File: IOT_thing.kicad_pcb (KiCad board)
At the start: 2 copper layers, 100 x 100 mm, 64 parts, among them J1 USB_C_Receptacle_USB2.0_16P, J2 Conn_01x04, J3 Screw_Terminal_01x03, J4 Screw_Terminal_01x08, J5 Screw_Terminal_01x02, J6 Conn_02x05_Odd_Even, K1 RT314A05, Q1 UMH3N, Q2 UMH3N, Q3 BC817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

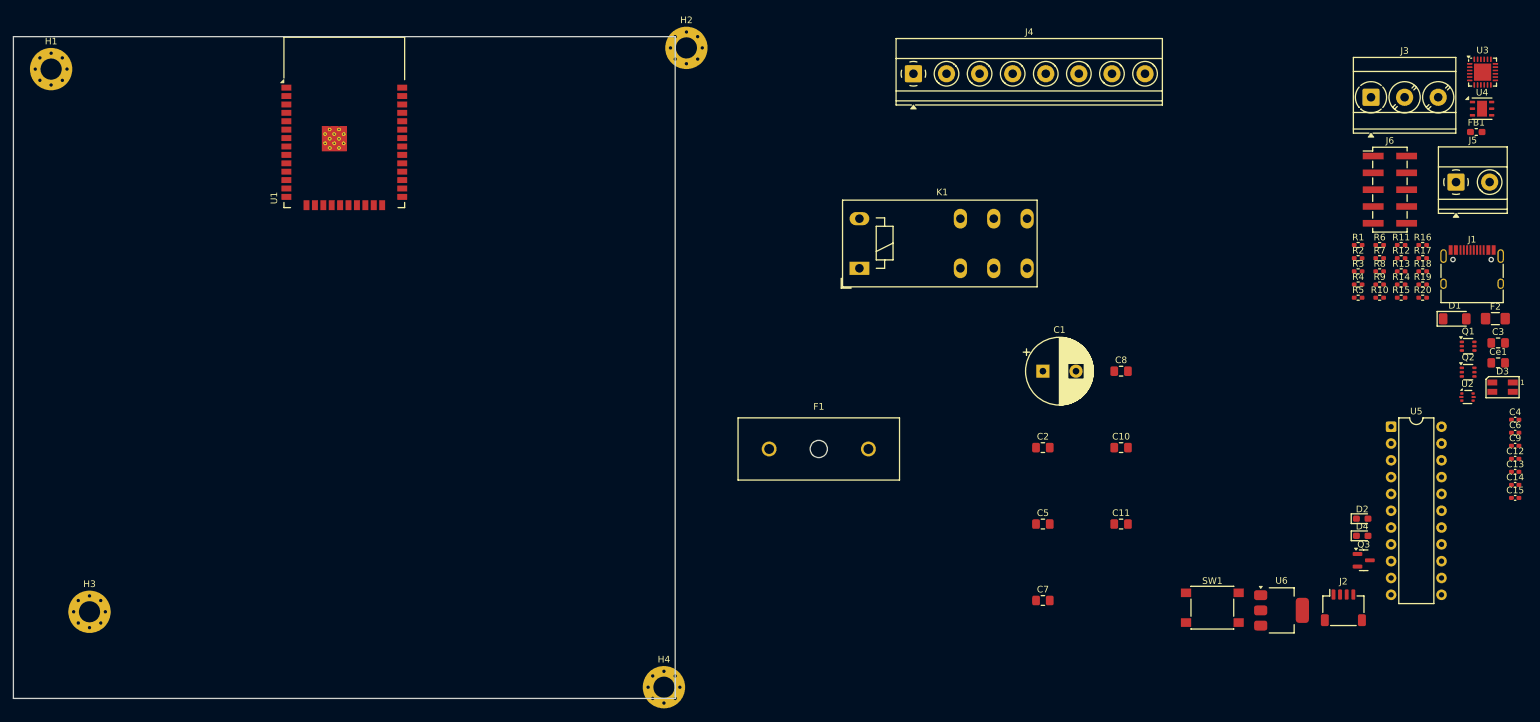
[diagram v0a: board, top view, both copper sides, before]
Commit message: Updated some footprints and 3d models
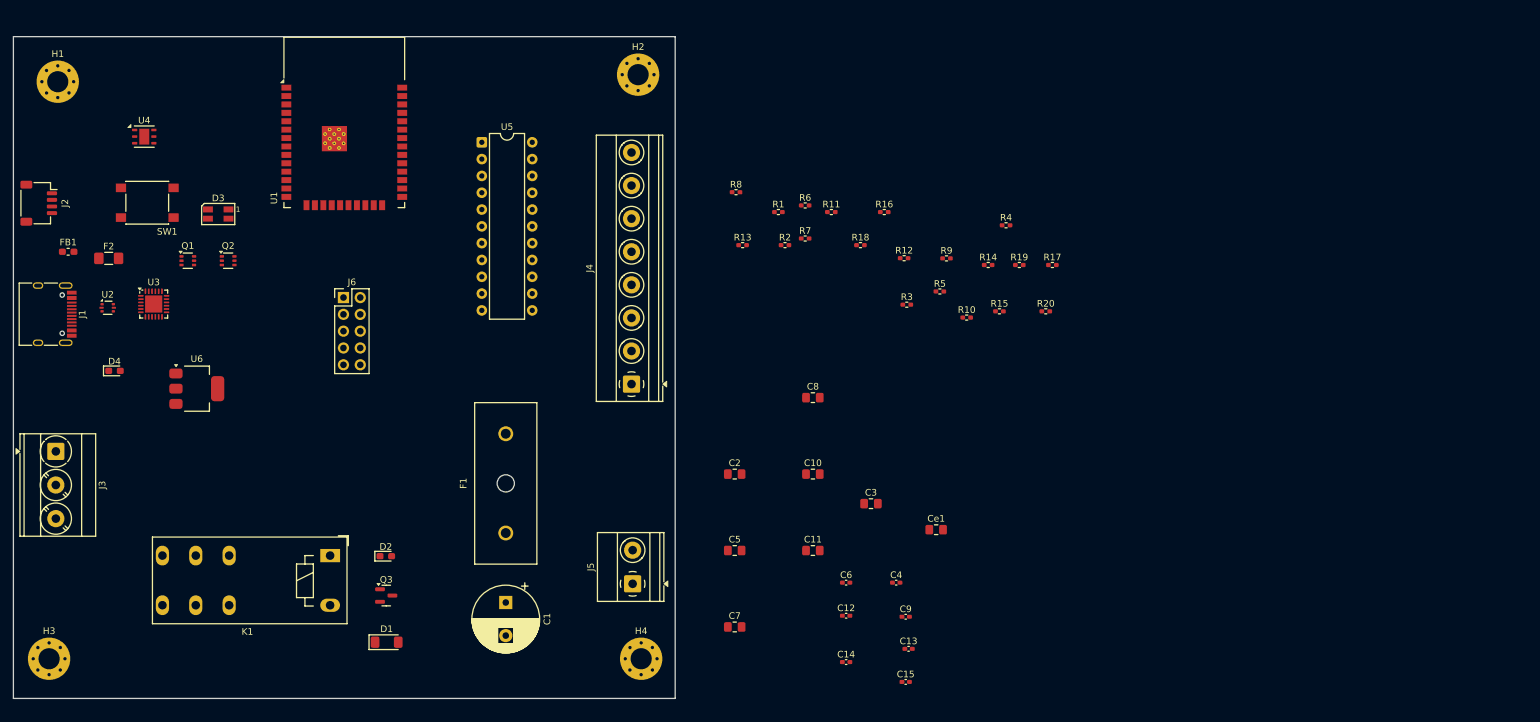
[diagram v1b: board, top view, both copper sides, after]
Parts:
- F1: footprint Fuse:FUSE_696105003002 -> iot-thing_Library_11:FUSE_696105003002
- J6: footprint Connector_PinHeader_2.54mm:PinHeader_2x05_P2.54mm_Vertical_SMD -> iot-thing_Library_11:PinHeader_2x05_P2.54mm_Vertical
- SW1: footprint Button_Switch_SMD1:SW_Push_1P1T_NO_6x6mm_H9.5mm -> iot-thing_Library_11:SW_Push_1P1T_NO_6x6mm_H9.5mm
- moved J1 215.7 mm to (63.4, 89.4), turned to -90 degrees
- moved FB1 213.5 mm to (66.9, 80.0)
- moved F2 209.7 mm to (73.0, 81.0)
- moved J2 206.4 mm to (62.4, 72.7), turned to -90 degrees
- moved U2 205.9 mm to (72.8, 88.5)
- moved J3 205.8 mm to (65.0, 110.2), turned to -90 degrees
- moved U3 203.8 mm to (79.8, 87.9)
- moved U4 202.2 mm to (78.4, 62.6)
- moved D3 195.8 mm to (89.5, 74.3)
- moved Q1 193.9 mm to (85.0, 81.3)
- moved D4 190.2 mm to (73.9, 98.0)
- moved Q2 188.1 mm to (91.0, 81.3)
- moved SW1 172.2 mm to (78.8, 72.6)
- moved D1 168.6 mm to (115.0, 139.0)
- moved U6 167.3 mm to (86.3, 100.7)
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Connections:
- Q1 pad 3: (no net) -> /IO0
- Q1 pad 4: (no net) -> /DTR
- Q1 pad 5: (no net) -> /RTS
- Q2 pad 3: (no net) -> /RTS
- Q2 pad 4: (no net) -> +3.3V
- Q2 pad 5: (no net) -> /DTR
